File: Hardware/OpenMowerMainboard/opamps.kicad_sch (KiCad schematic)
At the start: 19 parts, among them U12 MCP604

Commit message: added footprints to schematic
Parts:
- added unit 4 of U12
- C1, C3, C5: footprint ene9ba_footprint:C050-025X075 -> Capacitor_SMD:C_0805_2012Metric_Pad1.18x1.45mm_HandSolder
- R44, R45, R46, R47, R48, R49, R50, R53, R55, R57: footprint Resistor_THT:R_Axial_DIN0309_L9.0mm_D3.2mm_P12.70mm_Horizontal -> Resistor_SMD:R_0805_2012Metric_Pad1.20x1.40mm_HandSolder
- TP1, TP2, TP3, TP4, TP5: footprint (none) -> TestPoint:TestPoint_Pad_D2.0mm
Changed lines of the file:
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@@
     (property "Reference" "C5" (id 0) (at 165.735 170.815 90))
     (property "Value" "100n" (id 1) (at 167.005 168.275 90))
-    (property "Footprint" "ene9ba_footprint:C050-025X075" (id 2) (at 159.385 165.4302 0)
+    (property "Footprint" "Capacitor_SMD:C_0805_2012Metric_Pad1.18x1.45mm_HandSolder" (id 2) (at 159.385 165.4302 0)
       (effects (font (size 1.27 1.27)) hide)
     )
@@
       (effects (font (size 1.27 1.27)) (justify right))
     )
-    (property "Footprint" "" (id 2) (at 217.17 71.12 0)
+    (property "Footprint" "TestPoint:TestPoint_Pad_D2.0mm" (id 2) (at 217.17 71.12 0)
       (effects (font (size 1.27 1.27)) hide)
     )
@@
       (effects (font (size 1.27 1.27)) (justify left))
     )
-    (property "Footprint" "Resistor_THT:R_Axial_DIN0309_L9.0mm_D3.2mm_P12.70mm_Horizontal" (id 2) (at 98.552 78.74 90)
+    (property "Footprint" "Resistor_SMD:R_0805_2012Metric_Pad1.20x1.40mm_HandSolder" (id 2) (at 98.552 78.74 90)
       (effects (font (size 1.27 1.27)) hide)
     )
@@
       (effects (font (size 1.27 1.27)) (justify left))
     )
-    (property "Footprint" "Resistor_THT:R_Axial_DIN0309_L9.0mm_D3.2mm_P12.70mm_Horizontal" (id 2) (at 92.71 69.088 90)
+    (property "Footprint" "Resistor_SMD:R_0805_2012Metric_Pad1.20x1.40mm_HandSolder" (id 2) (at 92.71 69.088 90)
       (effects (font (size 1.27 1.27)) hide)
     )
@@
       (effects (font (size 1.27 1.27)) (justify right))
     )
-    (property "Footprint" "" (id 2) (at 119.38 69.85 0)
+    (property "Footprint" "TestPoint:TestPoint_Pad_D2.0mm" (id 2) (at 119.38 69.85 0)
       (effects (font (size 1.27 1.27)) hide)
     )
@@
     (property "Reference" "C3" (id 0) (at 213.36 96.52 90))
     (property "Value" "100n" (id 1) (at 214.63 93.98 90))
-    (property "Footprint" "ene9ba_footprint:C050-025X075" (id 2) (at 207.01 91.1352 0)
+    (property "Footprint" "Capacitor_SMD:C_0805_2012Metric_Pad1.18x1.45mm_HandSolder" (id 2) (at 207.01 91.1352 0)
       (effects (font (size 1.27 1.27)) hide)
     )
@@
       (effects (font (size 1.27 1.27)) (justify right))
     )
-    (property "Footprint" "" (id 2) (at 172.085 88.265 0)
+    (property "Footprint" "TestPoint:TestPoint_Pad_D2.0mm" (id 2) (at 172.085 88.265 0)
       (effects (font (size 1.27 1.27)) hide)
     )
@@
       (effects (font (size 1.27 1.27)) (justify right))
     )
-    (property "Footprint" "" (id 2) (at 171.45 68.58 0)
+    (property "Footprint" "TestPoint:TestPoint_Pad_D2.0mm" (id 2) (at 171.45 68.58 0)
       (effects (font (size 1.27 1.27)) hide)
     )
@@
       (effects (font (size 1.27 1.27)) (justify left))
     )
-    (property "Footprint" "ene9ba_footprint:C050-025X075" (id 2) (at 195.2752 76.2 0)
+    (property "Footprint" "Capacitor_SMD:C_0805_2012Metric_Pad1.18x1.45mm_HandSolder" (id 2) (at 195.2752 76.2 0)
       (effects (font (size 1.27 1.27)) hide)
     )
@@
     (pin "4")
   )
+  (symbol (lib_id "Amplifier_Operational:MCP604") (at 118.745 97.155 0) (unit 4)
+    (in_bom yes) (on_board yes) (fields_autoplaced)
+    (property "Reference" "U12" (id 0) (at 118.745 86.36 0))
+    (property "Value" "MCP604" (id 1) (at 118.745 88.9 0))
+    (property "Footprint" "Package_SO:SOIC-14_3.9x8.7mm_P1.27mm" (id 2) (at 117.475 94.615 0)
+      (effects (font (size 1.27 1.27)) hide)
+    )
+    (property "Datasheet" "http://ww1.microchip.com/downloads/en/DeviceDoc/21314g.pdf" (id 3) (at 120.015 92.075 0)
+      (effects (font (size 1.27 1.27)) hide)
+    )
+    (pin "12")
+    (pin "13")
+    (pin "14")
+  )
   (symbol (lib_id "Device:R") (at 186.69 68.58 270) (unit 1)
     (in_bom yes) (on_board yes)
@@
       (effects (font (size 1.27 1.27)) (justify left))
     )
-    (property "Footprint" "Resistor_THT:R_Axial_DIN0309_L9.0mm_D3.2mm_P12.70mm_Horizontal" (id 2) (at 186.69 66.802 90)
+    (property "Footprint" "Resistor_SMD:R_0805_2012Metric_Pad1.20x1.40mm_HandSolder" (id 2) (at 186.69 66.802 90)
       (effects (font (size 1.27 1.27)) hide)
     )
@@
       (effects (font (size 1.27 1.27)) (justify left))
     )
-    (property "Footprint" "Resistor_THT:R_Axial_DIN0309_L9.0mm_D3.2mm_P12.70mm_Horizontal" (id 2) (at 98.552 58.42 90)
+    (property "Footprint" "Resistor_SMD:R_0805_2012Metric_Pad1.20x1.40mm_HandSolder" (id 2) (at 98.552 58.42 90)
       (effects (font (size 1.27 1.27)) hide)
     )
@@
       (effects (font (size 1.27 1.27)) (justify left))
     )
-    (property "Footprint" "Resistor_THT:R_Axial_DIN0309_L9.0mm_D3.2mm_P12.70mm_Horizontal" (id 2) (at 51.308 76.2 90)
+    (property "Footprint" "Resistor_SMD:R_0805_2012Metric_Pad1.20x1.40mm_HandSolder" (id 2) (at 51.308 76.2 90)
       (effects (font (size 1.27 1.27)) hide)
     )
@@
       (effects (font (size 1.27 1.27)) (justify right))
     )
-    (property "Footprint" "" (id 2) (at 92.71 67.31 0)
+    (property "Footprint" "TestPoint:TestPoint_Pad_D2.0mm" (id 2) (at 92.71 67.31 0)
       (effects (font (size 1.27 1.27)) hide)
     )
@@
       (effects (font (size 1.27 1.27)) (justify left))
     )
-    (property "Footprint" "Resistor_THT:R_Axial_DIN0309_L9.0mm_D3.2mm_P12.70mm_Horizontal" (id 2) (at 74.93 79.502 90)
+    (property "Footprint" "Resistor_SMD:R_0805_2012Metric_Pad1.20x1.40mm_HandSolder" (id 2) (at 74.93 79.502 90)
       (effects (font (size 1.27 1.27)) hide)
     )
@@
       (effects (font (size 1.27 1.27)) (justify left))
     )
-    (property "Footprint" "Resistor_THT:R_Axial_DIN0309_L9.0mm_D3.2mm_P12.70mm_Horizontal" (id 2) (at 111.76 51.562 90)
+    (property "Footprint" "Resistor_SMD:R_0805_2012Metric_Pad1.20x1.40mm_HandSolder" (id 2) (at 111.76 51.562 90)
       (effects (font (size 1.27 1.27)) hide)
     )
@@
       (effects (font (size 1.27 1.27)) (justify left))
     )
-    (property "Footprint" "Resistor_THT:R_Axial_DIN0309_L9.0mm_D3.2mm_P12.70mm_Horizontal" (id 2) (at 59.69 83.058 90)
+    (property "Footprint" "Resistor_SMD:R_0805_2012Metric_Pad1.20x1.40mm_HandSolder" (id 2) (at 59.69 83.058 90)
       (effects (font (size 1.27 1.27)) hide)
     )
@@
       (effects (font (size 1.27 1.27)) (justify left))
     )
-    (property "Footprint" "Resistor_THT:R_Axial_DIN0309_L9.0mm_D3.2mm_P12.70mm_Horizontal" (id 2) (at 210.82 79.502 90)
+    (property "Footprint" "Resistor_SMD:R_0805_2012Metric_Pad1.20x1.40mm_HandSolder" (id 2) (at 210.82 79.502 90)
       (effects (font (size 1.27 1.27)) hide)
     )
@@
       (effects (font (size 1.27 1.27)) (justify left))
     )
-    (property "Footprint" "Resistor_THT:R_Axial_DIN0309_L9.0mm_D3.2mm_P12.70mm_Horizontal" (id 2) (at 198.12 79.502 90)
-      (effects (font (size 1.27 1.27)) hide)
-    )
+    (property "Footprint" "Resistor_SMD:R_0805_2012Metric_Pad1.20x1.40mm_HandSolder" (id 2) (at 198.12 79.502 90)
+      (effects (font (size 1.27 1.27)) hide)
+    )

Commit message: wip
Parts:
- removed C3: 100n, Capacitor_SMD:C_0805_2012Metric_Pad1.18x1.45mm_HandSolder, symbol Device:C
- removed R53, R55: 1k5, Resistor_SMD:R_0805_2012Metric_Pad1.20x1.40mm_HandSolder, symbol Device:R
- removed R57: 27k, Resistor_SMD:R_0805_2012Metric_Pad1.20x1.40mm_HandSolder, symbol Device:R
- removed TP3, TP4: TestPoint, TestPoint:TestPoint_Pad_D2.0mm, symbol Connector:TestPoint
- removed U12: MCP604, Package_SO:SOIC-14_3.9x8.7mm_P1.27mm, symbol Amplifier_Operational:MCP604
- added D13: D_Schottky, Diode_SMD:D_SOD-123F, symbol Device:D_Schottky
- added D14: D_Zener, Diode_SMD:D_SOD-123F, symbol Device:D_Zener
- added IC2: TSC101CILT, TSC101CILT:SOT95P280X145-5N, symbol TSC101CILT:TSC101CILT
- added U? (x5): MCP604, symbol Amplifier_Operational:MCP604
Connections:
- net +3V3: now also D13.1 (K), U?.4 (V+)
- net CHARGE_CURRENT: now also D13.2 (A), D14.1 (K), IC2.1 (OUT)
- net GND: now also C1.2, D14.2 (A), IC2.2 (GND), U?.10 (+), U?.11 (V-), U?.12 (+), U?.13 (-), U?.9 (-)
- net RAIN-: now also U?.3 (+)
- net RAIN_DETECTED: now also U?.7
- net SHUNT_CHARGE_CURRENT+: now also IC2.3 (VP)
- net SHUNT_CHARGE_CURRENT-: now also IC2.4 (VM); no longer C1.2
- net at R45.2, R46.2: now also U?.2 (-)
- net at R46.1, R47.1: now also U?.1
- net +5V: now reaches C1.1
- net +5V: now also IC2.5 (VCC)
- net at R48.1, R49.1: now also U?.6 (-)
- net at R47.2, R50.1, TP2.1: now also U?.5 (+)
- no-connect marks 0 -> 2
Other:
- note removed: "Ladestrom 6 A == 5V"
- moved on the sheet: TP5

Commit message: wip pcb layout
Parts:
- U2: renamed from U?; footprint (none) -> Package_SO:SOIC-14_3.9x8.7mm_P1.27mm
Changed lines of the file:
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@@
   (symbol (lib_id "power:GND") (at 72.39 139.7 0) (unit 1)
     (in_bom yes) (on_board yes)
-    (property "Reference" "#PWR?" (id 0) (at 72.39 146.05 0)
+    (property "Reference" "#PWR0162" (id 0) (at 72.39 146.05 0)
       (effects (font (size 1.27 1.27)) hide)
     )
@@
   (symbol (lib_id "Amplifier_Operational:MCP604") (at 87.63 127 0) (unit 4)
     (in_bom yes) (on_board yes) (fields_autoplaced)
-    (property "Reference" "U?" (id 0) (at 87.63 116.205 0))
+    (property "Reference" "U2" (id 0) (at 87.63 116.205 0))
     (property "Value" "MCP604" (id 1) (at 87.63 118.745 0))
-    (property "Footprint" "" (id 2) (at 86.36 124.46 0)
+    (property "Footprint" "Package_SO:SOIC-14_3.9x8.7mm_P1.27mm" (id 2) (at 86.36 124.46 0)
       (effects (font (size 1.27 1.27)) hide)
     )
@@
   (symbol (lib_id "Amplifier_Operational:MCP604") (at 74.93 67.31 0) (unit 1)
     (in_bom yes) (on_board yes) (fields_autoplaced)
-    (property "Reference" "U?" (id 0) (at 74.93 57.15 0))
+    (property "Reference" "U2" (id 0) (at 74.93 57.15 0))
     (property "Value" "MCP604" (id 1) (at 74.93 59.69 0))
-    (property "Footprint" "" (id 2) (at 73.66 64.77 0)
+    (property "Footprint" "Package_SO:SOIC-14_3.9x8.7mm_P1.27mm" (id 2) (at 73.66 64.77 0)
       (effects (font (size 1.27 1.27)) hide)
     )
@@
   (symbol (lib_id "Amplifier_Operational:MCP604") (at 114.3 69.85 0) (unit 2)
     (in_bom yes) (on_board yes) (fields_autoplaced)
-    (property "Reference" "U?" (id 0) (at 114.3 59.69 0))
+    (property "Reference" "U2" (id 0) (at 114.3 59.69 0))
     (property "Value" "MCP604" (id 1) (at 114.3 62.23 0))
-    (property "Footprint" "" (id 2) (at 113.03 67.31 0)
+    (property "Footprint" "Package_SO:SOIC-14_3.9x8.7mm_P1.27mm" (id 2) (at 113.03 67.31 0)
       (effects (font (size 1.27 1.27)) hide)
     )
@@
   (symbol (lib_id "Amplifier_Operational:MCP604") (at 87.63 111.125 0) (unit 3)
     (in_bom yes) (on_board yes) (fields_autoplaced)
-    (property "Reference" "U?" (id 0) (at 87.63 100.33 0))
+    (property "Reference" "U2" (id 0) (at 87.63 100.33 0))
     (property "Value" "MCP604" (id 1) (at 87.63 102.87 0))
-    (property "Footprint" "" (id 2) (at 86.36 108.585 0)
+    (property "Footprint" "Package_SO:SOIC-14_3.9x8.7mm_P1.27mm" (id 2) (at 86.36 108.585 0)
       (effects (font (size 1.27 1.27)) hide)
     )
@@
   (symbol (lib_id "Amplifier_Operational:MCP604") (at 155.575 169.545 0) (unit 5)
     (in_bom yes) (on_board yes) (fields_autoplaced)
-    (property "Reference" "U?" (id 0) (at 153.67 168.2749 0)
+    (property "Reference" "U2" (id 0) (at 153.67 168.2749 0)
       (effects (font (size 1.27 1.27)) (justify left))
     )
@@
       (effects (font (size 1.27 1.27)) (justify left))
     )
-    (property "Footprint" "" (id 2) (at 154.305 167.005 0)
-      (effects (font (size 1.27 1.27)) hide)
-    )
+    (property "Footprint" "Package_SO:SOIC-14_3.9x8.7mm_P1.27mm" (id 2) (at 154.305 167.005 0)
+      (effects (font (size 1.27 1.27)) hide)
+    )

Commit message: routing mostly done
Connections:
- net SHUNT_CHARGE_CURRENT+ renamed SHUNT_CHARGE_CURRENT_PLUS
- net SHUNT_CHARGE_CURRENT- renamed SHUNT_CHARGE_CURRENT_MINUS
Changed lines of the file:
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@@
     (effects (font (size 1.27 1.27)) (justify left))
   )
-  (hierarchical_label "SHUNT_CHARGE_CURRENT+" (shape input) (at 176.53 119.38 180)
+  (hierarchical_label "SHUNT_CHARGE_CURRENT_PLUS" (shape input) (at 176.53 119.38 180)
     (effects (font (size 1.27 1.27)) (justify right))
   )
-  (hierarchical_label "SHUNT_CHARGE_CURRENT-" (shape input) (at 226.06 114.3 0)
+  (hierarchical_label "SHUNT_CHARGE_CURRENT_MINUS" (shape input) (at 226.06 114.3 0)
     (effects (font (size 1.27 1.27)) (justify left))
   )

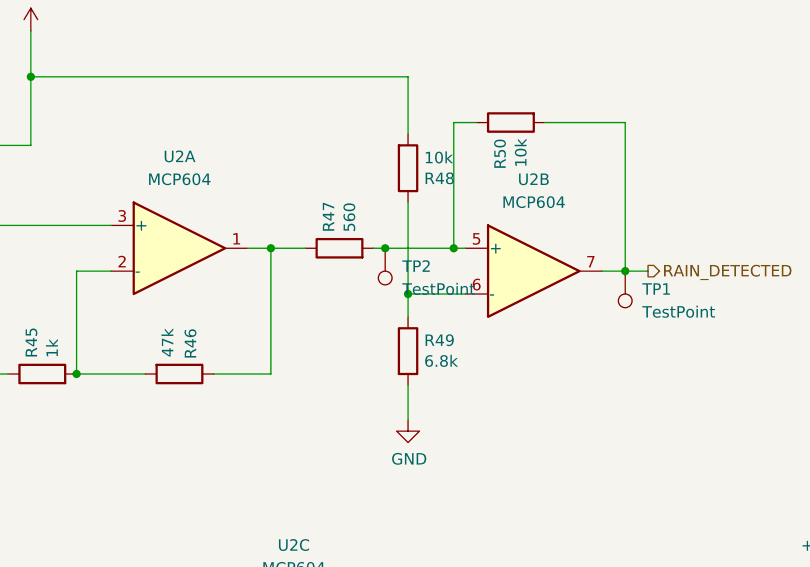
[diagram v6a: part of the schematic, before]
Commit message: update Resistance Values
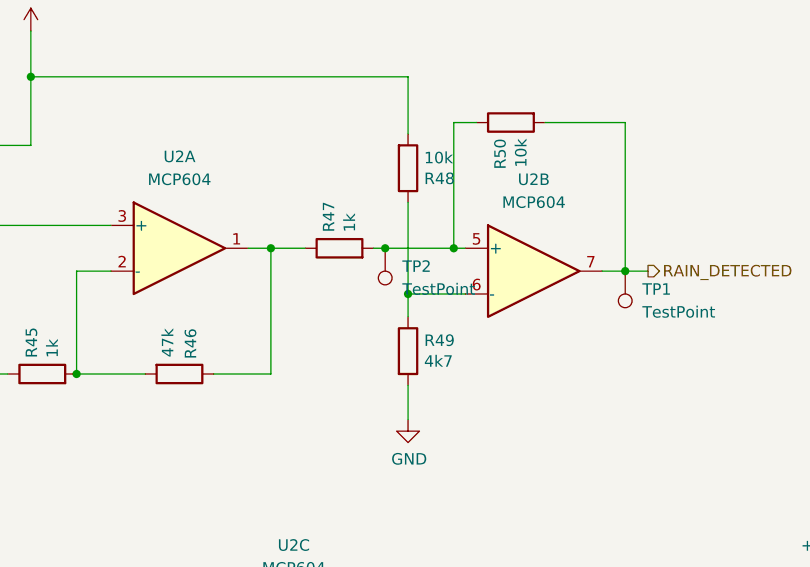
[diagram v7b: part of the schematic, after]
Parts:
- R47: value 560 -> 1k
- R49: value 6.8k -> 4k7
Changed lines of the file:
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@@
       (effects (font (size 1.27 1.27)) (justify left))
     )
-    (property "Value" "6.8k" (id 1) (at 102.108 79.883 0)
+    (property "Value" "4k7" (id 1) (at 102.108 79.883 0)
       (effects (font (size 1.27 1.27)) (justify left))
     )
@@
       (effects (font (size 1.27 1.27)) (justify left))
     )
-    (property "Value" "560" (id 1) (at 93.853 65.532 0)
+    (property "Value" "1k" (id 1) (at 93.853 65.532 0)
       (effects (font (size 1.27 1.27)) (justify left))
     )

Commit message: added some valued, exported iBOM
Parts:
- D13: value D_Schottky -> DNP
- D14: value D_Zener -> DNP
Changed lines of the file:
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@@
       (effects (font (size 1.27 1.27)) (justify left))
     )
-    (property "Value" "D_Zener" (id 1) (at 149.86 123.1899 90)
+    (property "Value" "DNP" (id 1) (at 149.86 123.1899 90)
       (effects (font (size 1.27 1.27)) (justify left))
     )
@@
       (effects (font (size 1.27 1.27)) (justify left))
     )
-    (property "Value" "D_Schottky" (id 1) (at 149.86 110.1724 90)
-      (effects (font (size 1.27 1.27)) (justify left))
-    )
+    (property "Value" "DNP" (id 1) (at 149.86 110.1724 90)
+      (effects (font (size 1.27 1.27)) (justify left))
+    )
